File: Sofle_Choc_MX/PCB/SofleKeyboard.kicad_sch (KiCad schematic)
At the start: 84 parts, among them J2 4PIN, J3 OLED, P1 i2c_pin, P2 i2c_pin, SW1 SW_PUSH_LED, SW10 SW_PUSH_LED, SW11 SW_PUSH_LED, SW12 SW_PUSH_LED, SW13 SW_PUSH_LED, SW14 SW_PUSH_LED, SW15 SW_PUSH_LED, SW16 SW_PUSH_LED, SW17 SW_PUSH_LED, SW18 SW_PUSH_LED, SW19 SW_PUSH_LED, SW2 SW_PUSH_LED, SW20 SW_PUSH_LED, SW21 SW_PUSH_LED, SW22 SW_PUSH_LED, SW23 SW_PUSH_LED, SW24 SW_PUSH_LED, SW25 Rotary_Encoder_Switch, SW26 SW_PUSH_LED, SW27 SW_PUSH_LED, SW28 SW_PUSH_LED, SW29 SW_PUSH_LED, SW3 SW_PUSH_LED, SW30 SW_PUSH_LED, SW4 SW_PUSH_LED, SW5 SW_PUSH_LED, SW6 SW_PUSH_LED, SW7 SW_PUSH_LED, SW8 SW_PUSH_LED, SW9 SW_PUSH_LED, U1 ProMicro

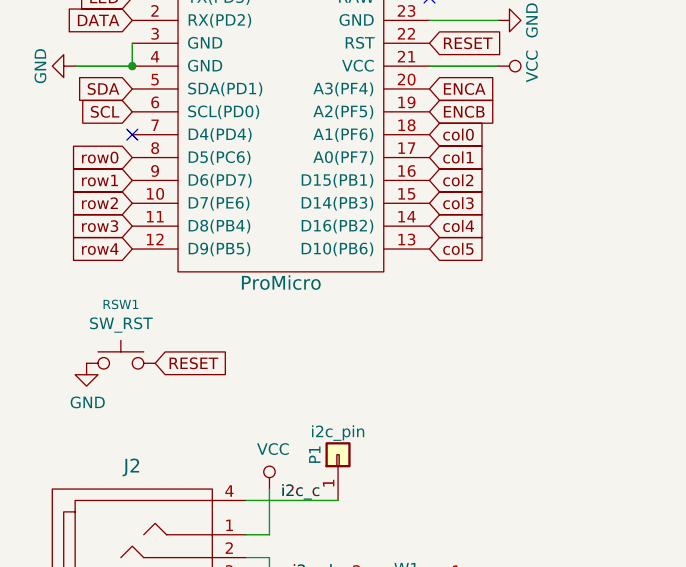
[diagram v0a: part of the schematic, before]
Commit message: Created TRRS footprint variant Poka-yoke by removing unnecessary trrs masks
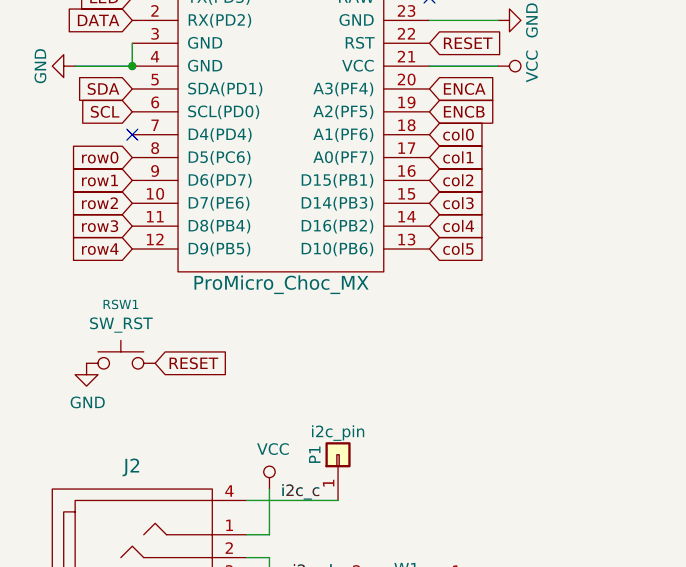
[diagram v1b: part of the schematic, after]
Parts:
- U1: value ProMicro -> ProMicro_Choc_MX; footprint SofleKeyboard-footprint:ProMicro -> SofleChoc:ProMicro_Choc_MX
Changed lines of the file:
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@@
     (stroke (width 0) (type default))
   )
-  (label "i2c_d" (at 45.72 86.36 0)
+  (label "i2c_d" (at 45.72 86.36 0) (fields_autoplaced)
     (effects (font (size 1.27 1.27)) (justify left bottom))
   )
-  (label "i2c_c" (at 44.45 77.47 0)
+  (label "i2c_c" (at 44.45 77.47 0) (fields_autoplaced)
     (effects (font (size 1.27 1.27)) (justify left bottom))
   )
@@
       (effects (font (size 1.524 1.524)))
     )
-    (property "Value" "ProMicro" (at 44.45 53.34 0)
+    (property "Value" "ProMicro_Choc_MX" (at 44.45 53.34 0)
       (effects (font (size 1.524 1.524)))
     )
-    (property "Footprint" "SofleKeyboard-footprint:ProMicro" (at 46.99 62.23 0)
+    (property "Footprint" "SofleChoc:ProMicro_Choc_MX" (at 46.99 62.23 0)
       (effects (font (size 1.524 1.524)) hide)
     )

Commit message: Sent this version out for production at jlcpcb
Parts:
- removed P1, P2: i2c_pin, SofleKeyboard-footprint:1pin_conn, symbol SofleKeyboard-rescue:i2c_pin-Lily58-cache-Lily58_Pro-rescue
- removed W1: jumper, SofleKeyboard-footprint:jumper_data, symbol SofleKeyboard-rescue:Jumper-Device
- added J1: Pimaroni Trackball, SofleChoc:Pimaroni_PinHeader_1x05_P2.54mm_Vertical, symbol Connector:Conn_01x05_Socket
- added J4: Unused, SofleChoc:1pin_conn, symbol Connector:Conn_01x01_Socket
- added J5: Conn_01x01_Socket, SofleChoc:1pin_conn, symbol Connector:Conn_01x01_Socket
- J2: footprint SofleKeyboard-footprint:MJ-4PP-9 -> SofleChoc:MJ-4PP-9_Choc_MX
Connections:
- net i2c_d is gone; now on net DATA: J2.3
- net DATA: now also J5.1 (Pin_1)
- net GND: now also J1.5 (Pin_5)
- net SCL: now also J1.3 (Pin_3)
- net SDA: now also J1.2 (Pin_2)
- net VCC: now also J1.1 (Pin_1)
- net i2c_c: no longer names the net of J2.4
- net i2c_c: now also J4.1 (Pin_1)
- no-connect marks 3 -> 4
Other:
- note added: "Pimaroni Trackball"
- moved on the sheet: J3, JP1, JP2, JP3, JP4, JP5, JP6, JP7, JP8

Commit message: Added double OLED footprint and removed jumpers
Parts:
- J3: footprint SofleKeyboard-footprint:OLED_4Pin -> SofleChoc:OLED_4Pin_Choc_MX
- R1, R2: footprint SofleKeyboard-footprint:RESISTOR_mini -> SofleChoc:R_I2C_bus
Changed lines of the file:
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@@
       (effects (font (size 1.27 1.27)))
     )
-    (property "Footprint" "SofleKeyboard-footprint:RESISTOR_mini" (at 70.612 96.52 90)
+    (property "Footprint" "SofleChoc:R_I2C_bus" (at 70.612 96.52 90)
       (effects (font (size 1.27 1.27)) hide)
     )
@@
       (effects (font (size 1.27 1.27)))
     )
-    (property "Footprint" "SofleKeyboard-footprint:RESISTOR_mini" (at 74.422 96.52 90)
+    (property "Footprint" "SofleChoc:R_I2C_bus" (at 74.422 96.52 90)
       (effects (font (size 1.27 1.27)) hide)
     )
@@
       (effects (font (size 1.27 1.27)))
     )
-    (property "Footprint" "SofleKeyboard-footprint:OLED_4Pin" (at 19.05 111.76 0)
-      (effects (font (size 1.27 1.27)) hide)
-    )
+    (property "Footprint" "SofleChoc:OLED_4Pin_Choc_MX" (at 19.05 111.76 0)
+      (effects (font (size 1.27 1.27)) hide)
+    )

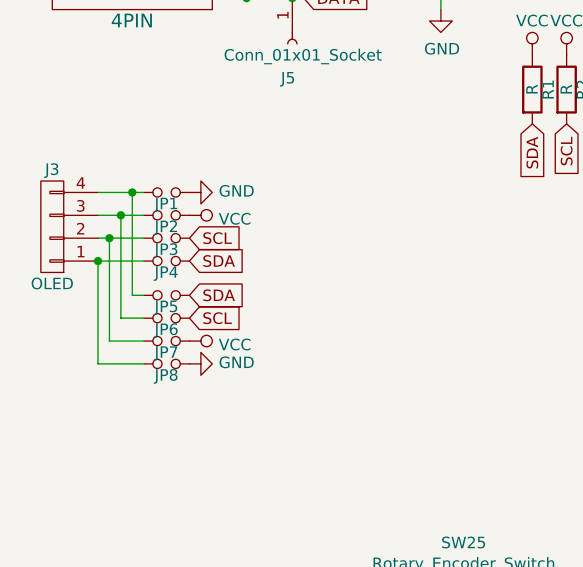
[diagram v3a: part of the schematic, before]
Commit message: OLED second socket added Updated schematic to remove jumpers for DS oled socket Increased Promicro footrprint spacing Cleaned up promicro routing Simplified promicro footprint for poke-yoke soldering
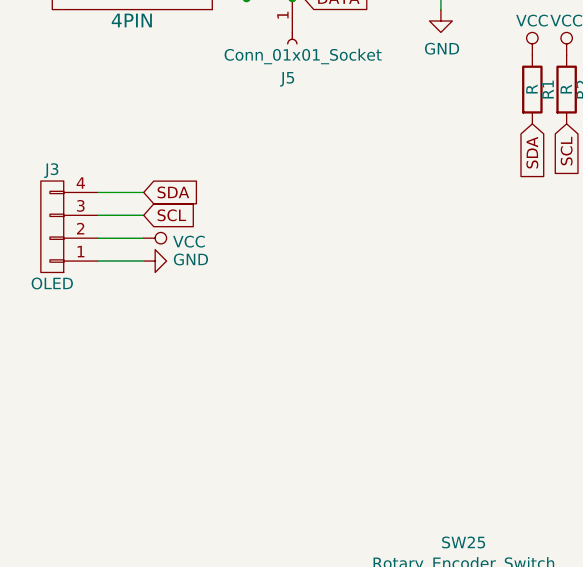
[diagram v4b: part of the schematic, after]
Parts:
- removed JP1, JP2, JP3, JP4, JP5, JP6, JP7, JP8: Jumper_NO_Small, SofleKeyboard-footprint:Jumper, symbol SofleKeyboard-rescue:Jumper_NO_Small-Device
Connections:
- net GND: now also J3.1 (P1)
- net SCL: now also J3.3 (P3)
- net SDA: now also J3.4 (P4)
- net VCC: now also J3.2 (P2)

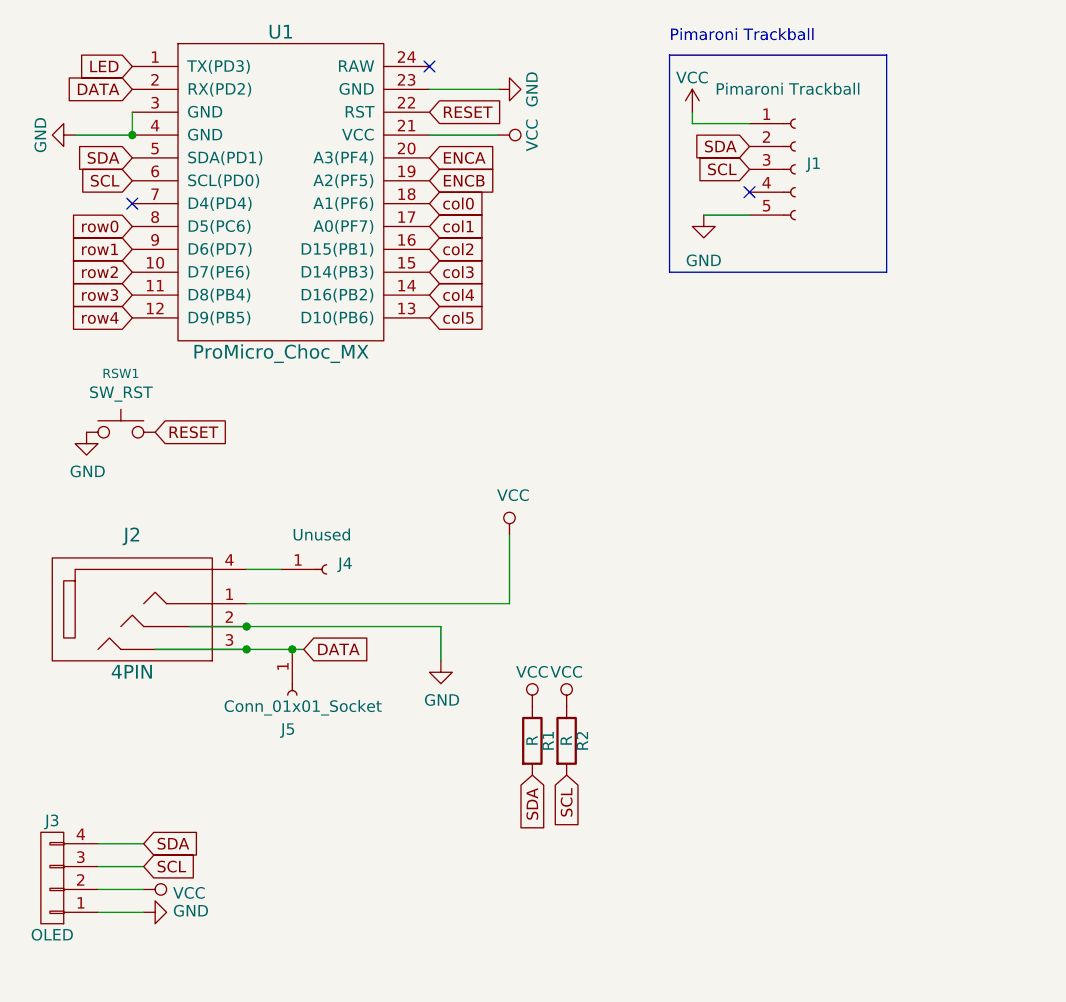
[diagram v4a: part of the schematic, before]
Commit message: Removed reset button added poke-yoke reset graphics Tweaked I2C component location
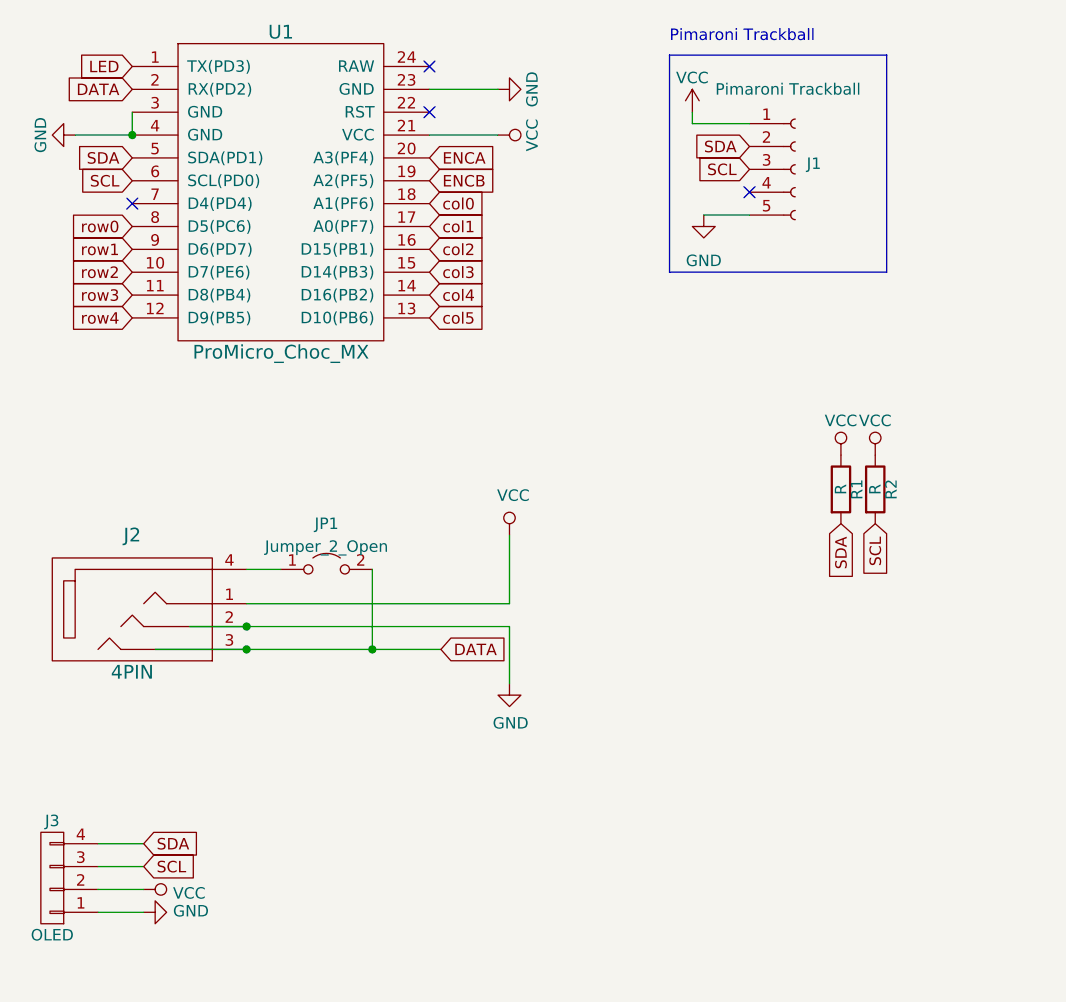
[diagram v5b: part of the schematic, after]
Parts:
- removed J4: Unused, SofleChoc:1pin_conn, symbol Connector:Conn_01x01_Socket
- removed J5: Conn_01x01_Socket, SofleChoc:1pin_conn, symbol Connector:Conn_01x01_Socket
- removed RSW1: SW_RST, SofleKeyboard-footprint:TACT_SWITCH_TVBP06, symbol SofleKeyboard-rescue:SW_RST-Lily58-cache-Lily58_Pro-rescue
- added JP1: Jumper_2_Open, symbol Jumper:Jumper_2_Open
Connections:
- net DATA: now also JP1.2 (B)
- net at J2.4: now also JP1.1 (A)
- net RESET: no longer names the net of U1.22 (RST)
- no-connect marks 4 -> 5
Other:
- moved on the sheet: R1, R2

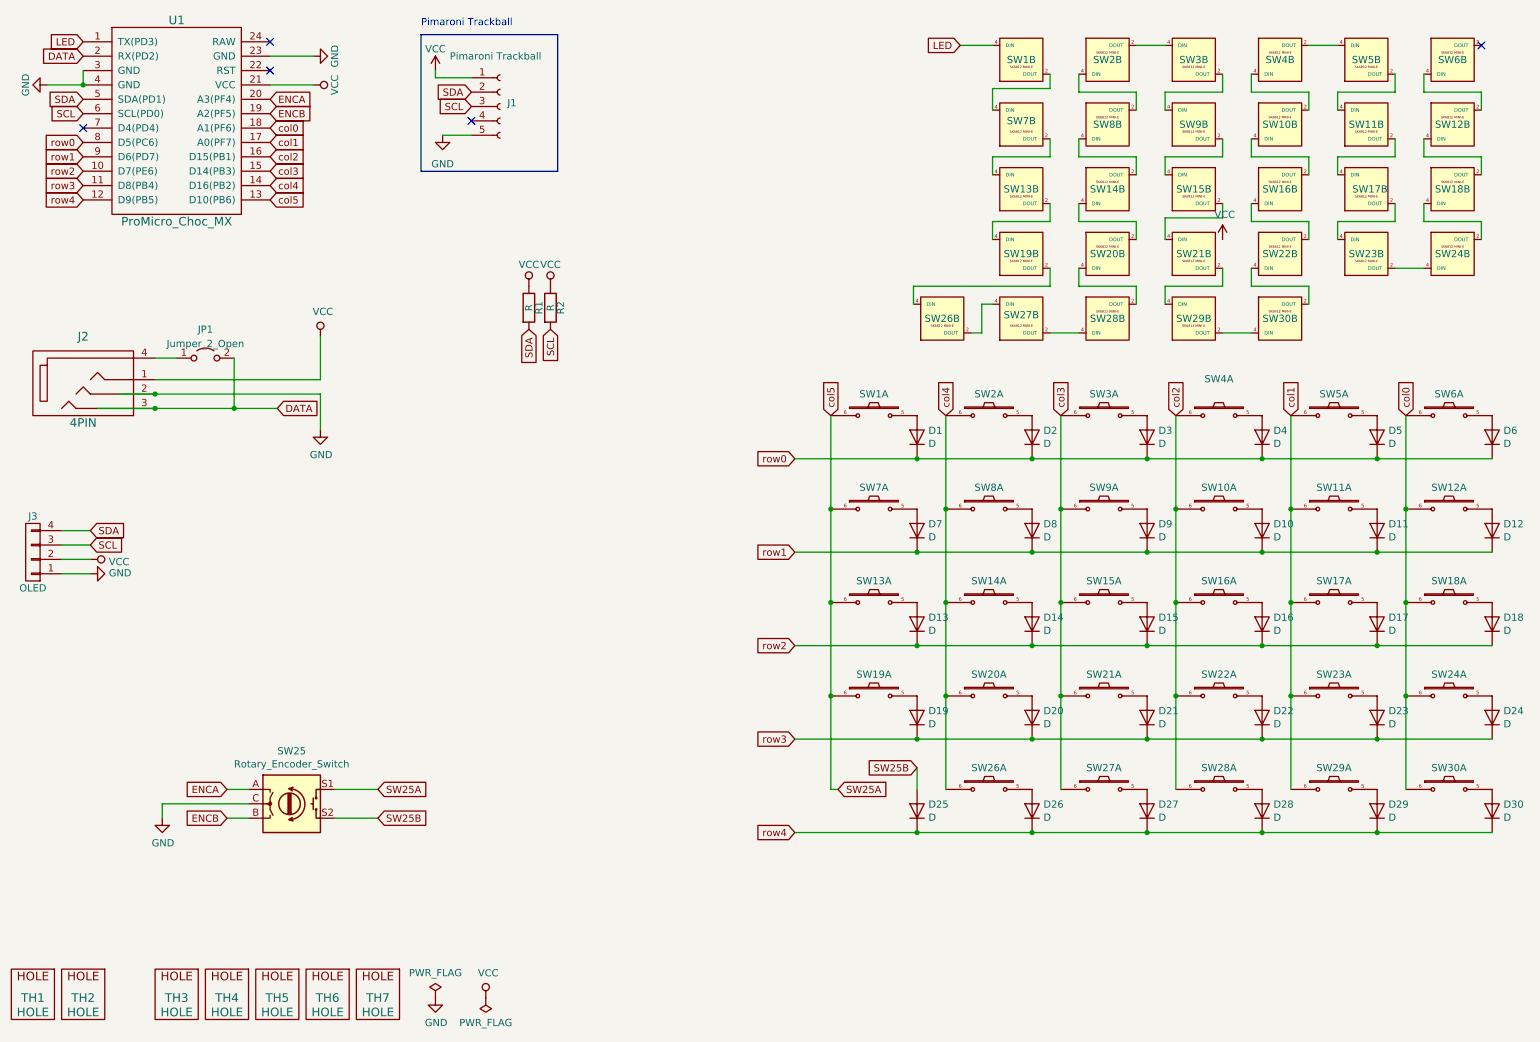
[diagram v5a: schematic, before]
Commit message: Fixed I2C bus rerouted and cleaned up teardrops labeleing tweaks DRC
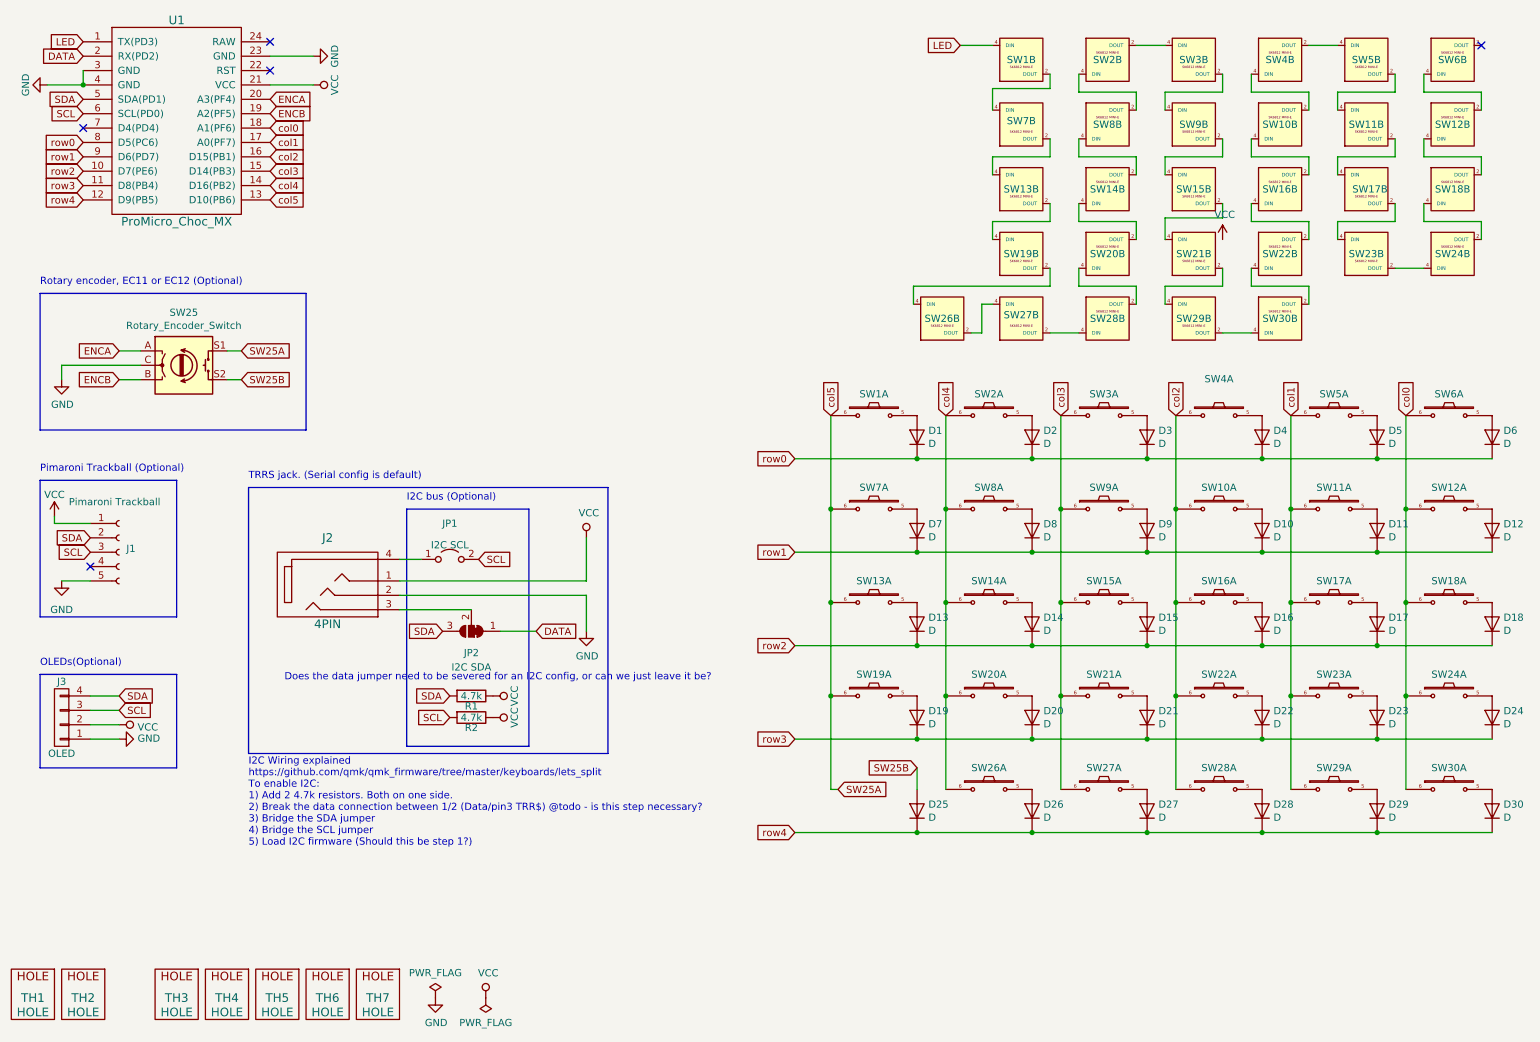
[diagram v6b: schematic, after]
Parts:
- added JP2: I2C SDA, Jumper:SolderJumper-3_P1.3mm_Bridged12_RoundedPad1.0x1.5mm_NumberLabels, symbol Jumper:SolderJumper_3_Bridged12
- J1: footprint SofleChoc:Pimaroni_PinHeader_1x05_P2.54mm_Vertical -> SofleChoc:pimoroni_trackball
- JP1: value Jumper_2_Open -> I2C SCL; footprint (none) -> Jumper:SolderJumper-2_P1.3mm_Open_RoundedPad1.0x1.5mm
- R1, R2: value R -> 4.7k
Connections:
- net DATA: now also JP2.1 (A); no longer J2.3, JP1.2 (B)
- net SCL: now also JP1.2 (B)
- net SDA: now also JP2.3 (B)
- new net: J2.3, JP2.2 (C)
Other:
- note added: "Does the data jumper need to be severed for an I2C config, or can we just leave it be?"
- note added: "I2C Wiring explained https://github.com/qmk/qmk_firmware/tree/master/keyboards/lets_split To enable I2C: 1) Add 2 4.7k resistors. Both on one side. 2) Break the data connection between 1/2 (Data/pin3 TRR$) @todo - is this step necessary? 3) Bridge the SDA jumper 4) Bridge the SCL jumper 5) Load I2C firmware (Should this be step 1?)"
- note added: "I2C bus (Optional)"
- note added: "OLEDs(Optional)"
- note added: "Pimaroni Trackball (Optional)"
- note added: "Rotary encoder, EC11 or EC12 (Optional)"
- note added: "TRRS jack. (Serial config is default)"
- note removed: "Pimaroni Trackball"
- moved on the sheet: J1, J2, J3, JP1, R1, R2, SW25
